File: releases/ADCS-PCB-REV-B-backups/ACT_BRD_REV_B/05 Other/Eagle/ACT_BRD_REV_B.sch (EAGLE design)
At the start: 228 parts, among them J11 TE_1-84953-1, J2 TE_1-84953-1, J4 TE_1-84953-1, J5 830-10-003-20-005000, U1 SIP2100DY-T1-GE3, U10 LM2917MX/NOPB, U12 TSV991AILT, U13 LM2917MX/NOPB, U14 ADS7841E_2K5, U16 DRV10970_MOTOR_DRIVERDRV10970, U17 LM2917MX/NOPB, U19 TSV991AILT, U2 SIP2100DY-T1-GE3, U20 ADS7841E_2K5, U3 SIP2100DY-T1-GE3, U6 DRV10970_MOTOR_DRIVERDRV10970, U7 DRV10970_MOTOR_DRIVERDRV10970, U8 TSV991AILT, U9 ADS7841E_2K5

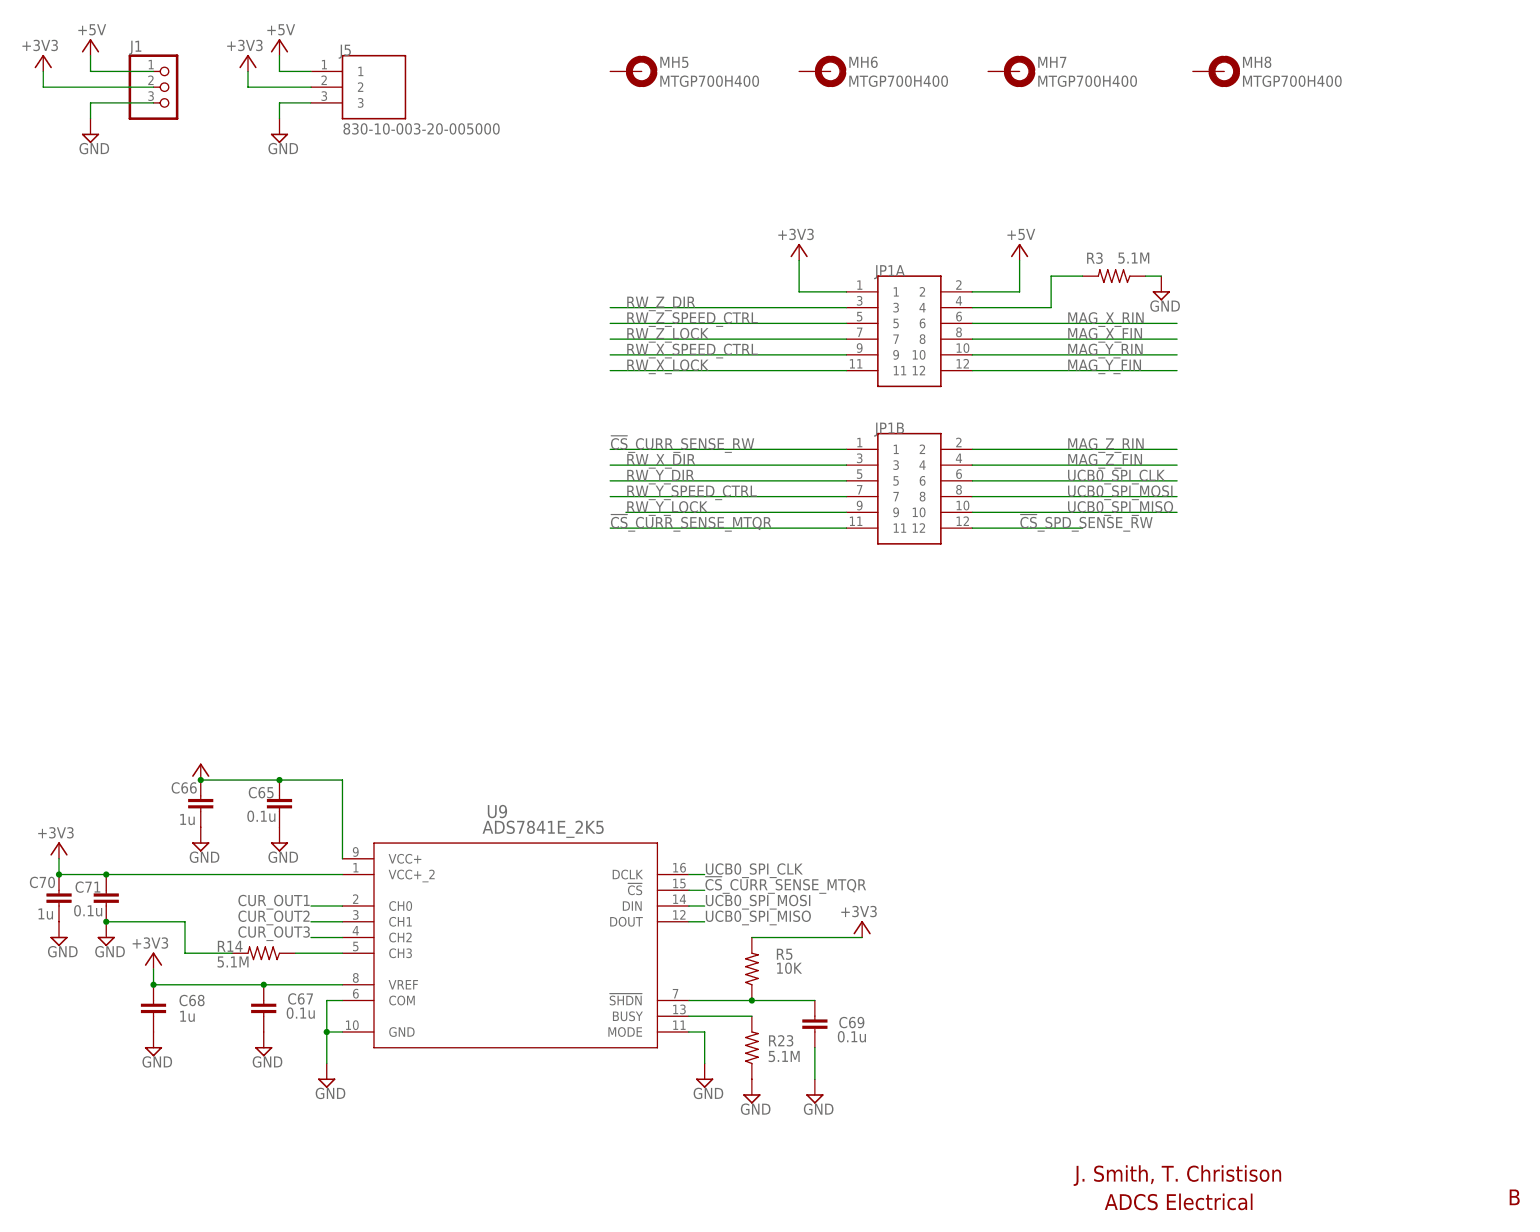
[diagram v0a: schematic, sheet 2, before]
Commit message: Finalized connectors for Luc and reattached burn wire
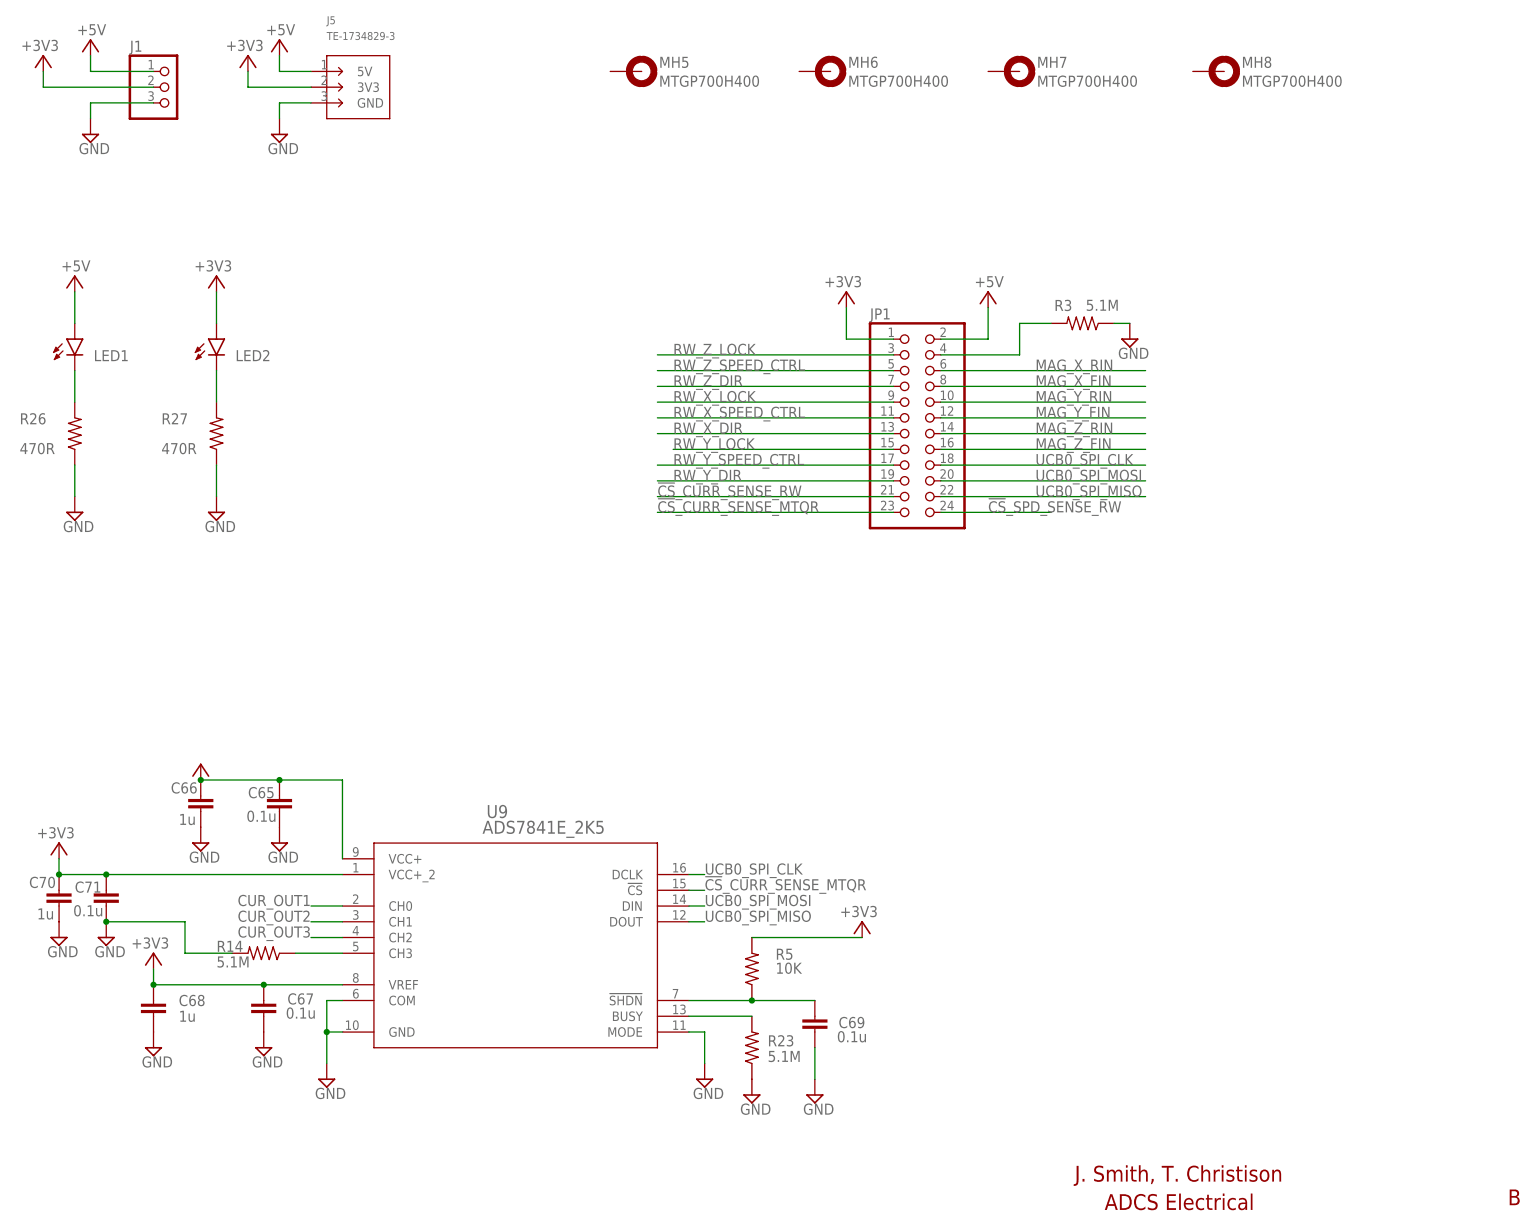
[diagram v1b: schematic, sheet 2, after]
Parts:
- removed JP1A, JP1B: 832-10-012-10-005000, 832-10-012-10-005000:832-10-012-10-005000
- added JP1: (no value), pinhead:PINHD-2X12
- added LED1, LED2: (no value), led:LEDCHIPLED_0603
- added R26, R27: 470R, rcl:R-US_R0603
- J5: value 830-10-003-20-005000 -> TE-1734829-3; device 830-10-003-20-005000:830-10-003-20-005000 -> my_library:TE-1734829-3
- R22, R42, R88: value 470R -> DNP
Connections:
- new net N$14: LED2.C, R27.2
- new net N$5: LED1.C, R26.2
- net !CS!_CURR_SENSE_MTQR: now also JP1.23; no longer JP1B.11
- net !CS!_CURR_SENSE_RW: now also JP1.21; no longer JP1B.1
- net !CS!_SPD_SENSE_RW: now also JP1.24; no longer JP1B.12
- net +3V3: now also J5.3V3, JP1.1, LED2.A; no longer J5.2, JP1A.1
- net +5V: now also J5.5V, JP1.2, LED1.A; no longer J5.1, JP1A.2
- net GND: now also J5.GND, R26.1, R27.1; no longer J5.3
- net MAG_X_FIN: now also JP1.8; no longer JP1A.8
- net MAG_X_RIN: now also JP1.6; no longer JP1A.6
- net MAG_Y_FIN: now also JP1.12; no longer JP1A.12
- net MAG_Y_RIN: now also JP1.10; no longer JP1A.10
- net MAG_Z_FIN: now also JP1.16; no longer JP1B.4
- net MAG_Z_RIN: now also JP1.14; no longer JP1B.2
- net N$1: now also JP1.4; no longer JP1A.4
- net RW_X_DIR: now also JP1.13; no longer JP1B.3
- net RW_X_LOCK: now also JP1.9; no longer JP1A.11
- net RW_X_SPEED_CTRL: now also JP1.11; no longer JP1A.9
- net RW_Y_DIR: now also JP1.19; no longer JP1B.5
- net RW_Y_LOCK: now also JP1.15; no longer JP1B.9
- net RW_Y_SPEED_CTRL: now also JP1.17; no longer JP1B.7
- net RW_Z_DIR: now also JP1.7; no longer JP1A.3
- net RW_Z_LOCK: now also JP1.3; no longer JP1A.7
- net RW_Z_SPEED_CTRL: now also JP1.5; no longer JP1A.5
- net UCB0_SPI_CLK: now also JP1.18; no longer JP1B.6
- net UCB0_SPI_MISO: now also JP1.22; no longer JP1B.10
- net UCB0_SPI_MOSI: now also JP1.20; no longer JP1B.8
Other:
- moved on the sheet: R3
